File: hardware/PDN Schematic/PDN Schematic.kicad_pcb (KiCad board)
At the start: 2 copper layers, 66 x 86 mm, 17 parts, among them J1 Conn_01x02_Pin, J10 Conn_01x02_Pin, J11 Led Indicator Pin, J2 Conn_01x02_Pin, J3 Conn_01x02_Pin, J4 Conn_01x04_Pin, J7 Conn_01x02_Pin, J8 Conn_01x02_Pin, J9 Conn_01x02_Pin, U1 Current Reader

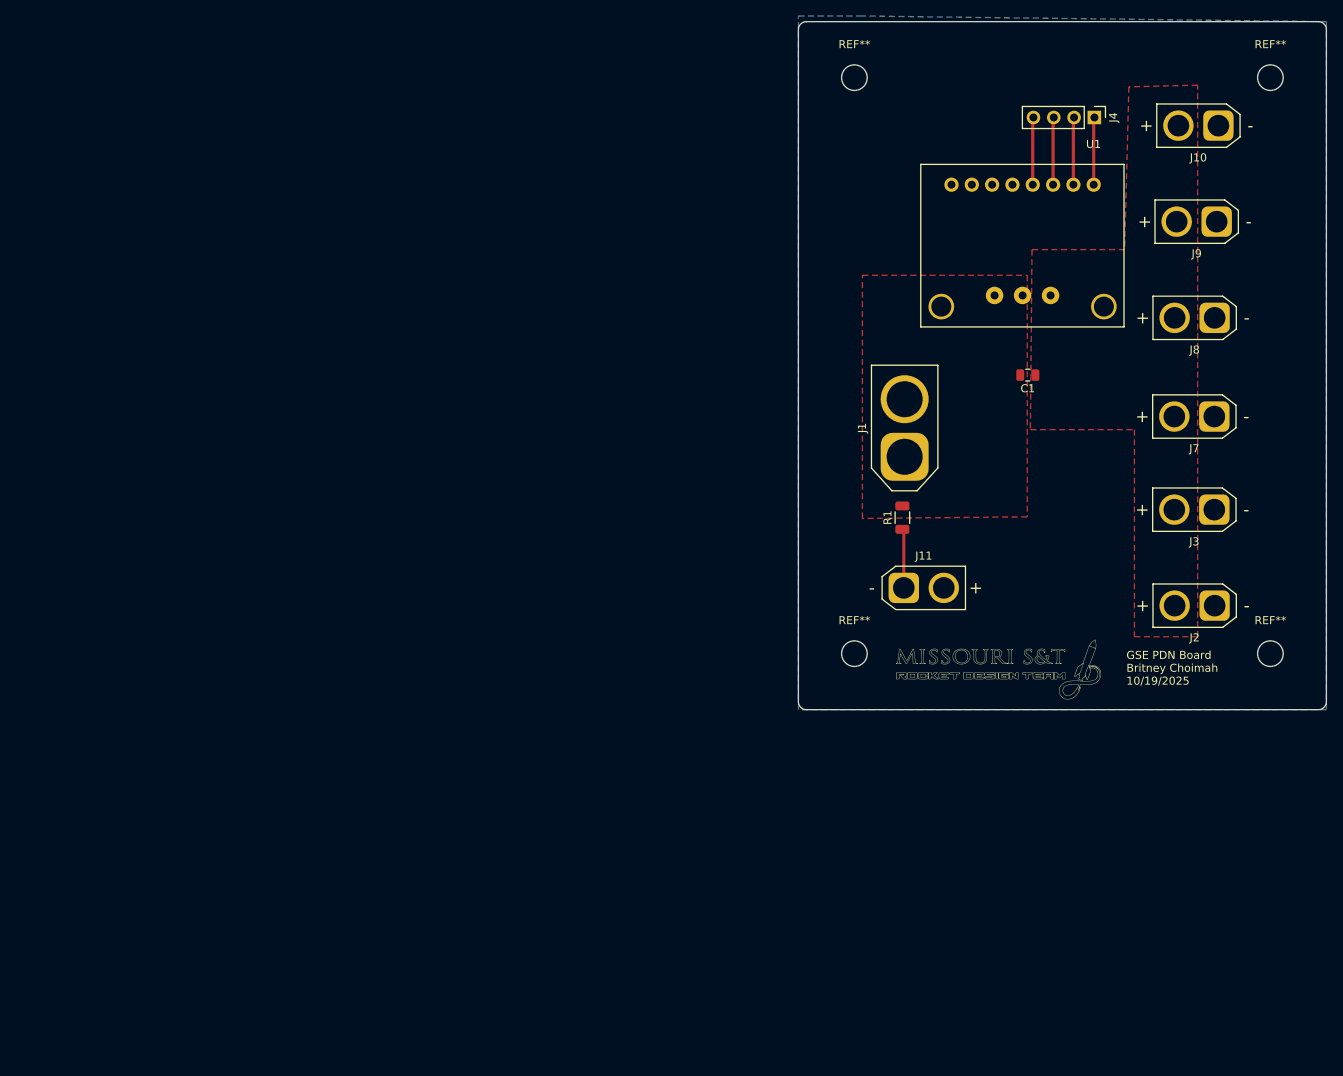
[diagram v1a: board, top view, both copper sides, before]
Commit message: Intermediate commit. DAQ code works occasionally (best after 15 mins of power off period!?!?). I think something isn't being configured correctly with the ADC
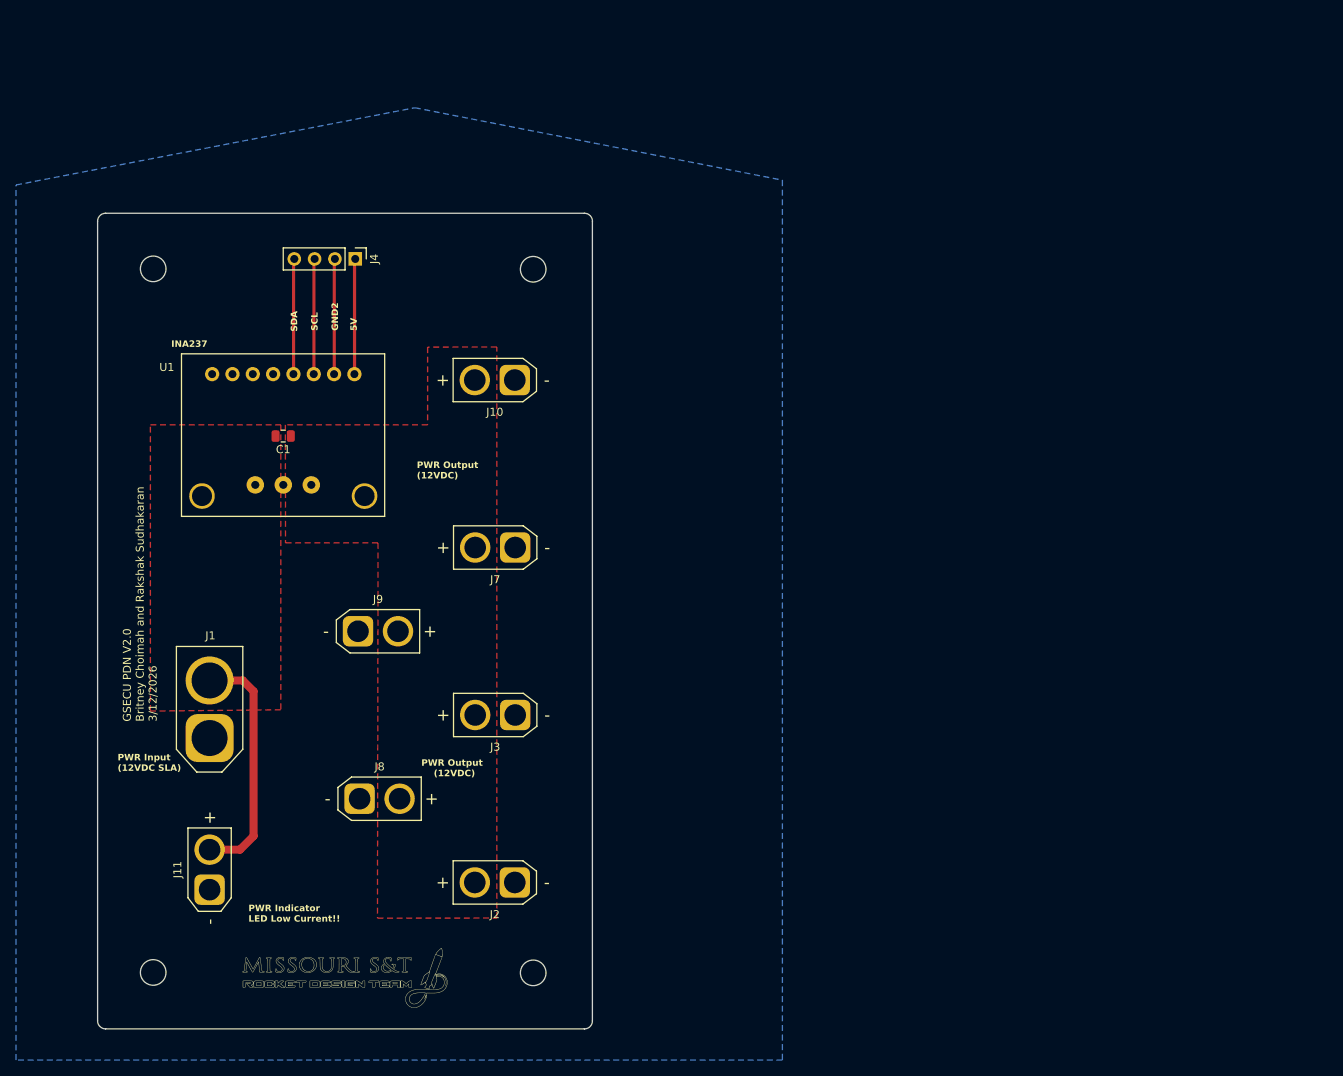
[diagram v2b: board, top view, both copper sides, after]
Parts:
- removed R1: 1k, Resistor_SMD:R_1206_3216Metric
- moved J8 122.6 mm to (95.2, 122.1), turned to 0 degrees
- moved J9 118.9 mm to (95.0, 101.2), turned to 0 degrees
- moved REF** 100.4 mm to (116.8, 143.9)
- moved REF** 96.3 mm to (69.3, 143.8)
- moved U1 95.4 mm to (94.5, 69.1)
- moved REF** 95.2 mm to (116.8, 56.0)
- moved J11 94.6 mm to (76.4, 133.5), turned to 90 degrees
- moved J2 94.1 mm to (114.5, 132.6)
- moved J4 94.1 mm to (94.6, 54.7)
- moved J1 93.7 mm to (76.4, 114.5)
- moved J10 93.5 mm to (114.5, 69.8)
- moved C1 93.4 mm to (85.6, 76.8)
- moved J3 91.1 mm to (114.6, 111.7)
- moved REF** 90.9 mm to (69.3, 55.9)
- moved G*** 90.3 mm to (93.3, 144.6)
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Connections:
- J1 pad 1: +13V -> GND
- J1 pad 2: GND -> +13V
- J11 pad 1: Net-(J11-Pin_1) -> GND
- J11 pad 2: GND -> +13V
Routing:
- net +13V: track 0.00 -> 30.4 mm
- net Net-(J11-Pin_1): track 7.39 -> 0.00 mm
- net Net-(J4-Pin_4): track 8.58 -> 14.6 mm
- net Net-(J4-Pin_3): track 8.58 -> 14.6 mm
- net Net-(J4-Pin_1): track 8.58 -> 14.6 mm
- net GND2: track 8.58 -> 14.6 mm
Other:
- board size 66 x 86 mm -> 61.9 x 102 mm
- board text added: "5V"
- board text added: "GND2"
- board text added: "GSECU PDN V2.0 Britney Choimah and Rakshak Sudhakaran 3/12/2026"
- board text added: "INA237"
- board text added: "PWR Indicator LED Low Current!!"
- board text added: "PWR Input (12VDC SLA)"
- board text added: "PWR Output (12VDC)"
- board text added: "SCL"
- board text added: "SDA"
- board text removed: "GSE PDN Board Britney Choimah 10/19/2025"
